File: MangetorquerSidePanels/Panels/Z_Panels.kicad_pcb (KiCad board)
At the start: 6 copper layers, 97 x 97.3 mm, 57 parts, among them J1 SMA Connector Male, J2 Through_Hole_1, Q1 BSS138DWQ-7, Q2 MBT2222ADW1T1, Q3 BSS138DWQ-7, Q4 MBT2222ADW1T1, U1 DRV8830DGQ, U2 BD60GC0WEFJ, U3 HHM1589D1, U4 OPT3001

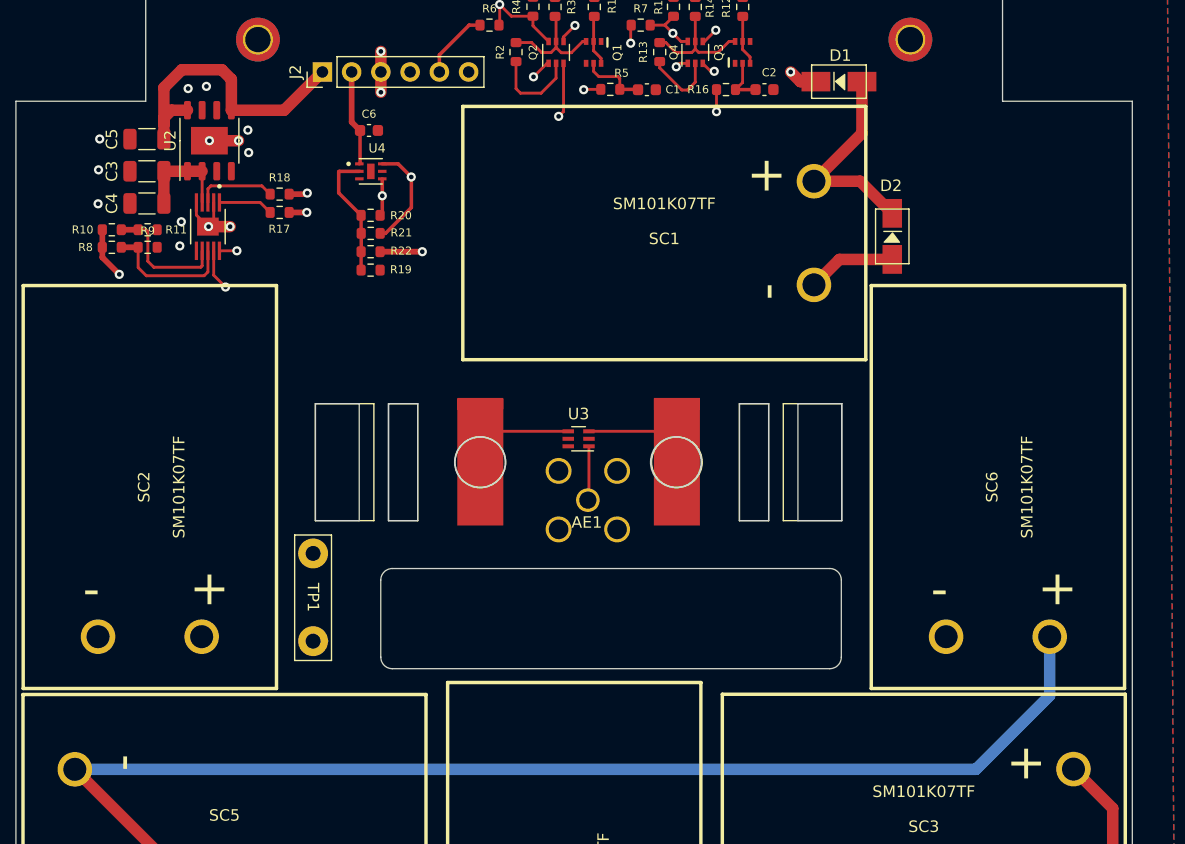
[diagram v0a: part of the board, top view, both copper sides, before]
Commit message: Starting design of magnetorquer side panels
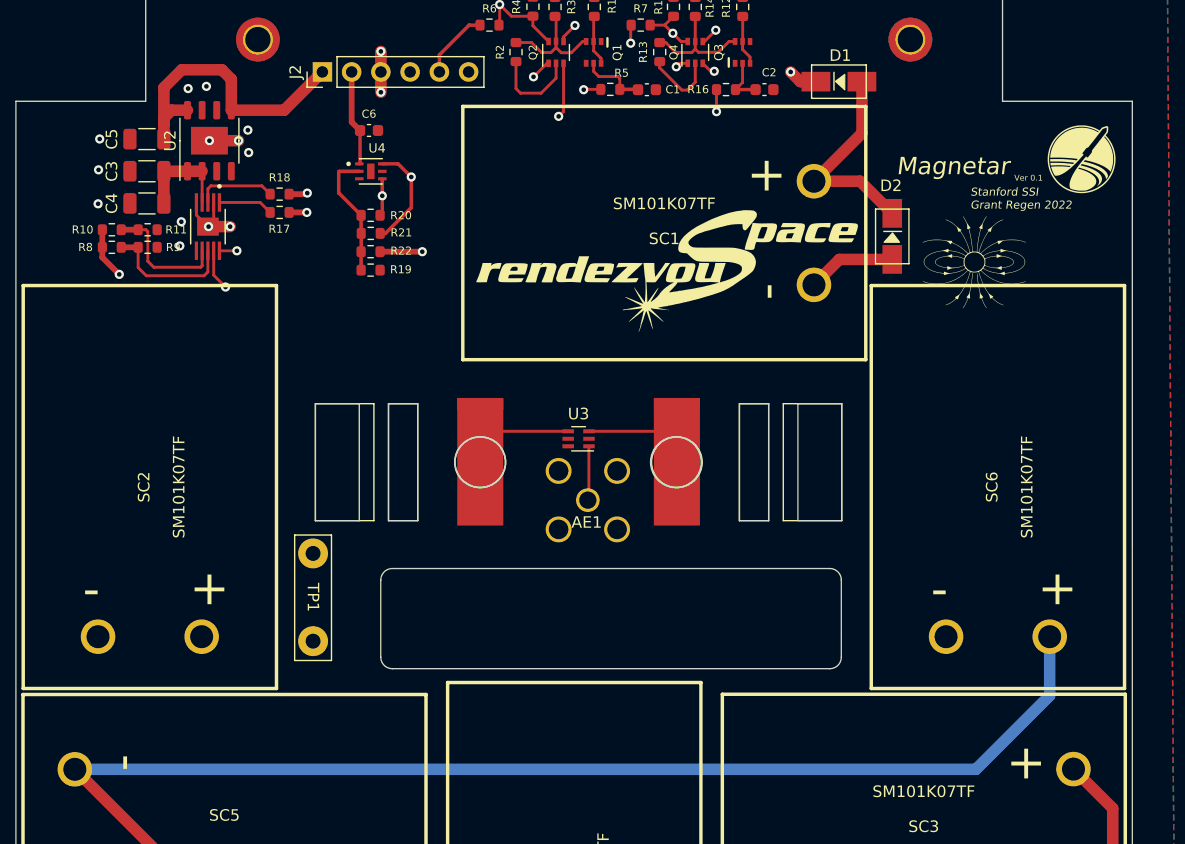
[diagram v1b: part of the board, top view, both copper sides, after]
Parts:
- added REF**: SLAB_logo, panels:SLAB_logo, F.Cu at (190.5, 64.8)
- added REF**: logo_SSI_small, panels:logo_SSI_small, F.Cu at (226.6, 56.6)
- added REF**: logo_magnet_1, panels:logo_magnet_1, F.Cu at (217.4, 65.3)
- added REF**: BAC_logo, panels:BAC_logo, B.Cu at (181.4, 125.5)
- added REF**: logo_SSI, panels:logo_SSI, B.Cu at (182.9, 62.2)
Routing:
- net Coil_OUT: track 46.1 -> 44.9 mm
- net Net-(D6-Pad2): track 123.7 -> 123.1 mm
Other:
- board text added: "Magnetar"
- board text added: "Stanford SSI Grant Regen 2022"
- board text added: "Ver 0.1"

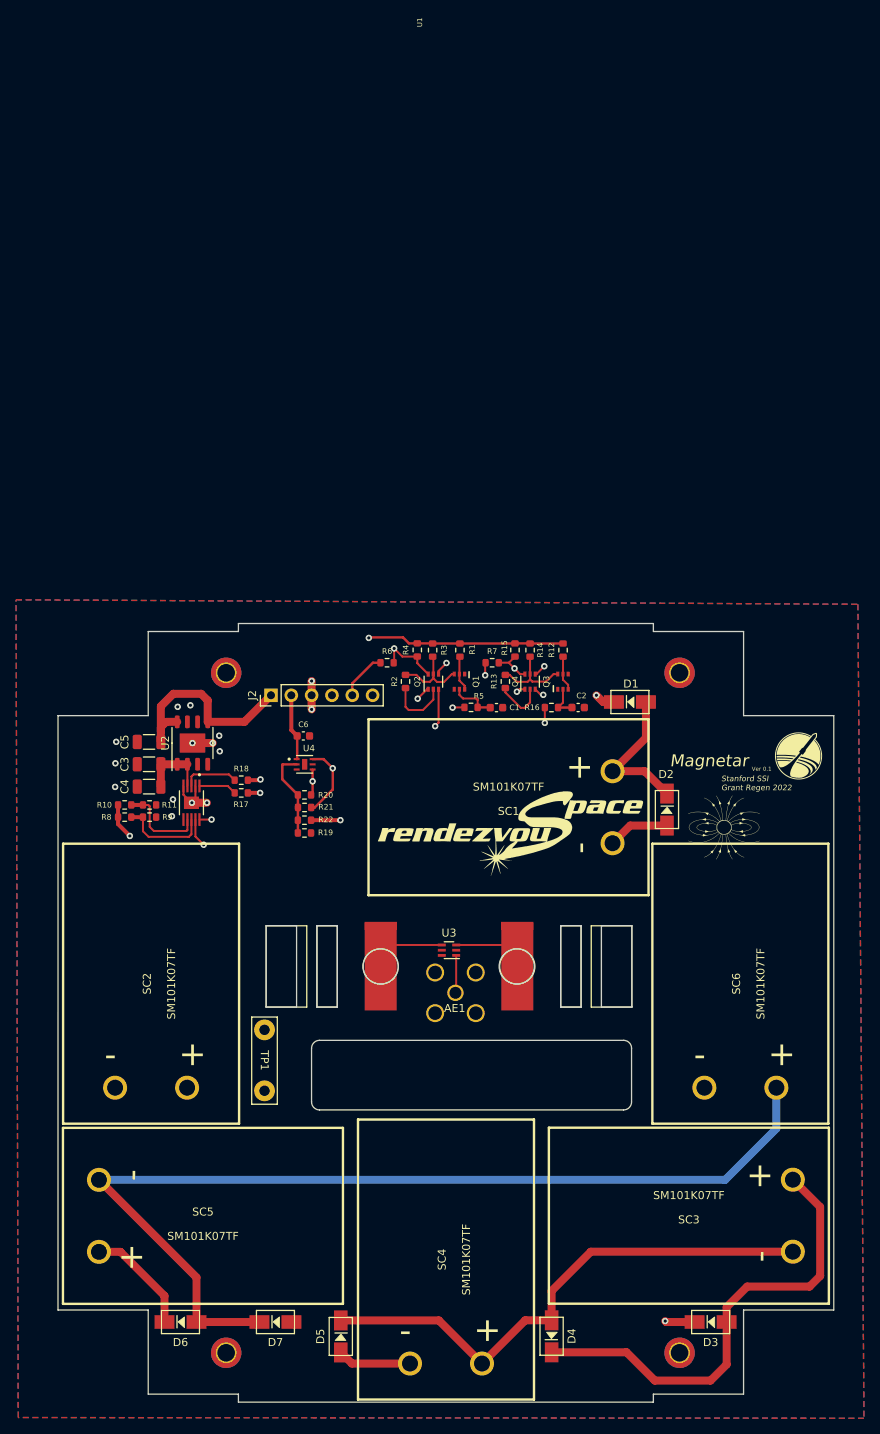
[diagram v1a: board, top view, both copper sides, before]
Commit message: Final flight side panels w/ magnetorquers finished, note final board thickness of 0.031'' and updated copper weight of 0.5oz for internal layers
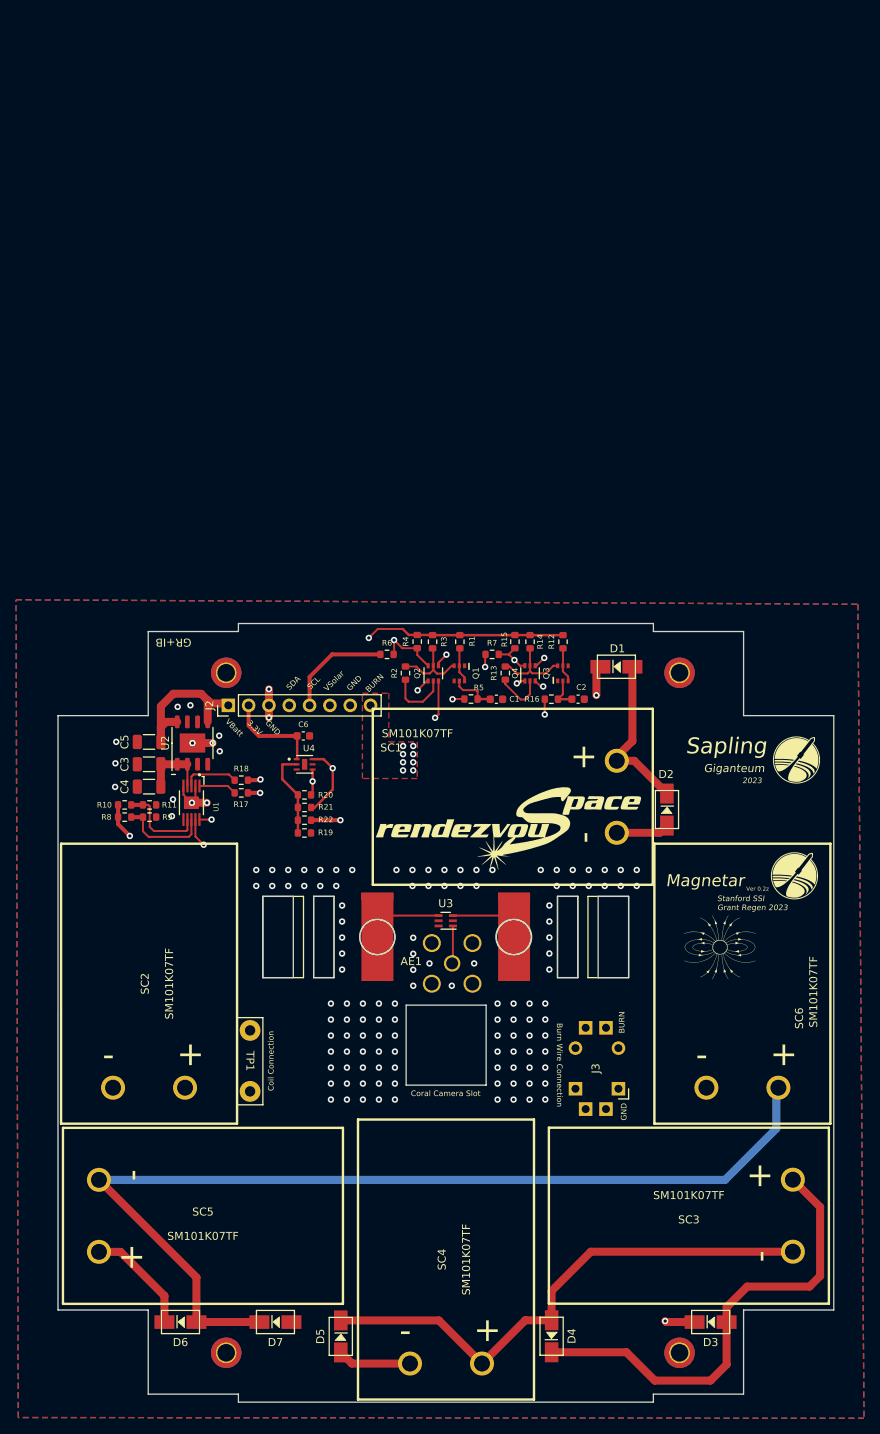
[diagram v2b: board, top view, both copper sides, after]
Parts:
- added J3: Conn_01x02, panels:Burn_Wire_Connection, F.Cu at (206.5, 101.8)
- added REF**: logo_SSI_small, panels:logo_SSI_small, F.Cu at (226.3, 57.1)
- J1: footprint sapling:SMA_Amphenol_901-144_Vertical -> panels:SMA_Amphenol_901-144_Vertical
- J2: value Through_Hole_1 -> Screw_Terminal_01x08; footprint Connector_PinHeader_2.54mm:PinHeader_1x06_P2.54mm_Vertical -> Connector_PinHeader_2.54mm:PinHeader_1x08_P2.54mm_Vertical
- U2: value BD60GC0WEFJ -> BD50GC0WEFJ
- moved REF** 15.0 mm to (226.1, 71.6)
- moved REF** 15.0 mm to (216.9, 80.3)
- moved J2 5.48 mm to (155.4, 50.0)
- moved D1 4.72 mm to (204.0, 45.2)
- moved AE1 3.70 mm to (182.6, 80.3)
- moved J1 3.70 mm to (183.4, 82.3)
- moved U3 3.70 mm to (182.6, 77.0)
- moved TP1 1.81 mm to (157.7, 94.5)
- moved SC1 1.40 mm to (191.0, 61.5)
- moved C2 1.04 mm to (199.2, 49.3)
- moved R1 1.04 mm to (184.4, 42.1)
- moved R12 1.04 mm to (197.3, 42.1)
- moved R14 1.04 mm to (193.2, 42.1)
- moved R16 1.04 mm to (195.8, 49.3)
- moved R3 1.04 mm to (181.0, 42.1)
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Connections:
- R10 pad 1: +3V3 -> VBATT
- R8 pad 1: +3V3 -> VBATT
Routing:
- net +3V3: track 110.3 -> 82.7 mm, vias 3 -> 2
- net VBATT: track 26.2 -> 48.3 mm, vias 0 -> 1
- net BURN: track 0.00 -> 14.0 mm, vias 0 -> 8
- net SCL: track 29.1 -> 41.3 mm
- net SDA: track 33.6 -> 40.8 mm
- net Net-(D1-Pad2): track 18.3 -> 21.3 mm
- net VSOLAR: track 41.0 -> 43.8 mm
- net Coil_IN: track 35.2 -> 32.9 mm
- net SCL_ISO: track 66.6 -> 67.7 mm
- net Coil_OUT: track 44.9 -> 44.2 mm
- net Net-(D2-Pad2): track 154.1 -> 154.6 mm
- net SDA_ISO: track 83.7 -> 84.2 mm
- net GND: vias 15 -> 133
- added copper zone on F.Cu, net BURN
- added copper zone on In3.Cu, net BURN
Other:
- outline, holes or cut-outs redrawn
- board text added: "2023"
- board text added: "3.3V"
- board text added: "BURN"
- board text added: "Burn Wire Connection"
- board text added: "Coil Connection"
- board text added: "Coral Camera Slot"
- board text added: "GND"
- board text added: "Giganteum"
- board text added: "SCL"
- board text added: "SDA"
- board text added: "Sapling"
- board text added: "Stanford SSI Grant Regen 2023"
- board text added: "VBatt"
- board text added: "VSolar"
- board text added: "Ver 0.2z"
- board text removed: "Stanford SSI Grant Regen 2022"
- board text removed: "Ver 0.1"

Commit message: added magnetorquers
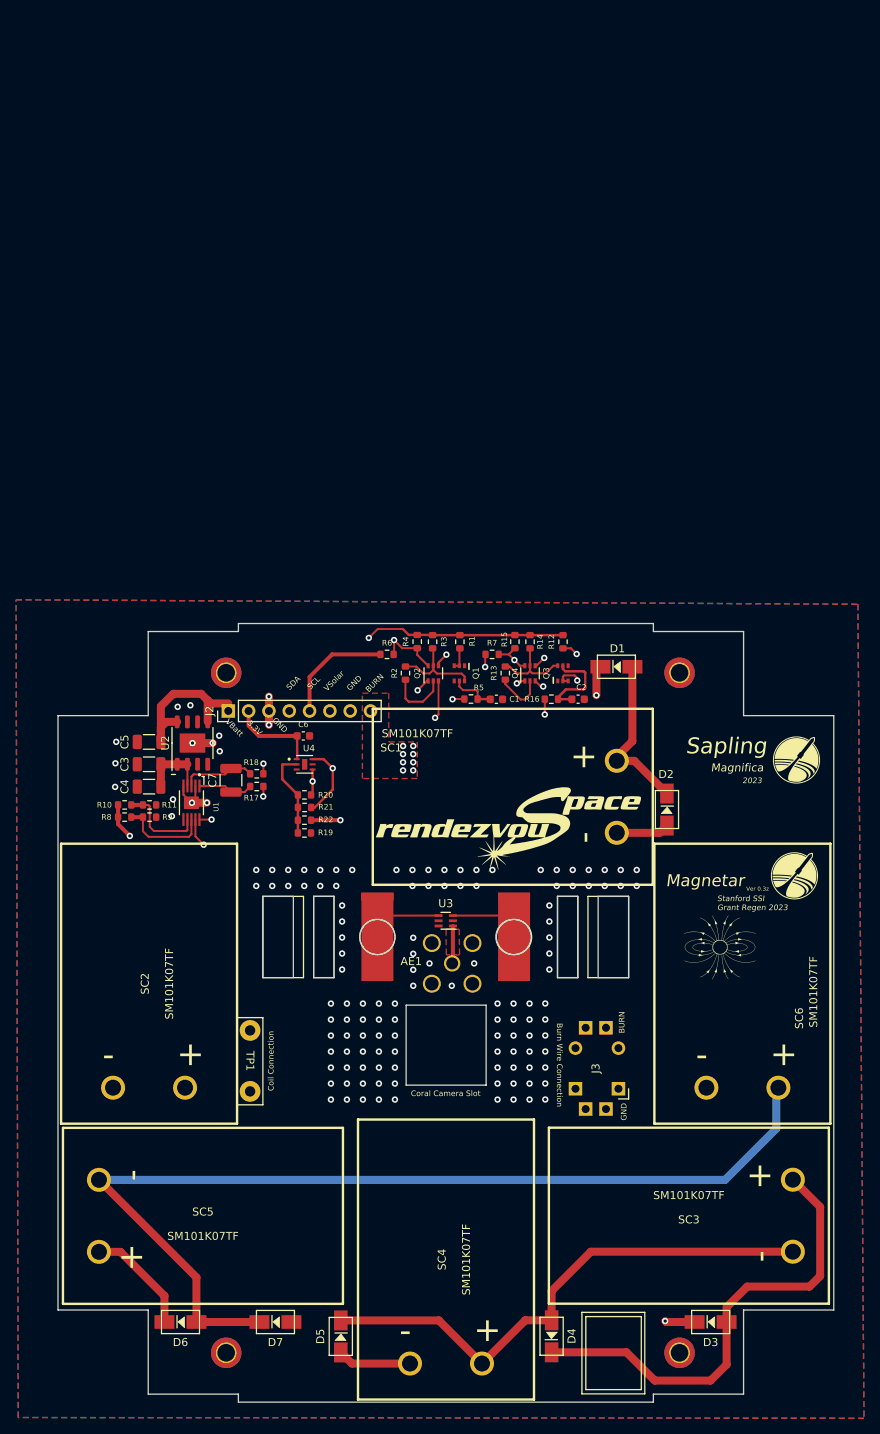
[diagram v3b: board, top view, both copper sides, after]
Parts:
- removed the REF** at (181.4, 125.5)
- added C7: XXuF, Capacitor_SMD:C_1210_3225Metric, F.Cu at (155.8, 59.4)
- moved R17 2.09 mm to (159.0, 60.2)
- moved R18 2.09 mm to (159.0, 58.6)
- moved J2 0.70 mm to (155.4, 50.7)
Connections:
- C2 pad 1: Net-(C2-Pad1) -> Net-(R16-Pad1)
- Q1 pad 2: Net-(Q1-Pad2) -> Net-(R1-Pad1)
- Q1 pad 3: Net-(Q1-Pad3) -> Net-(R1-Pad1)
- Q1 pad 6: Net-(Q1-Pad2) -> Net-(R3-Pad2)
- Q2 pad 5: Net-(Q1-Pad3) -> Net-(R3-Pad2)
- Q3 pad 2: Net-(C2-Pad1) -> Net-(Q3-Pad3)
- Q3 pad 5: Net-(Q3-Pad3) -> Net-(R16-Pad1)
- R1 pad 1: Net-(Q1-Pad2) -> Net-(R1-Pad1)
- R16 pad 1: Net-(C2-Pad1) -> Net-(R16-Pad1)
- R2 pad 1: Net-(Q1-Pad3) -> Net-(R3-Pad2)
- R3 pad 2: Net-(Q1-Pad3) -> Net-(R3-Pad2)
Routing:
- net Net-(R3-Pad2): track 0.00 -> 11.6 mm
- net Net-(R16-Pad1): track 0.00 -> 11.2 mm
- net Net-(Q1-Pad3): track 9.96 -> 0.00 mm
- net Net-(Q3-Pad3): track 4.35 -> 8.94 mm, vias 0 -> 2
- net Net-(Q1-Pad2): track 4.37 -> 0.00 mm
- net Net-(C2-Pad1): track 4.27 -> 0.00 mm
- net Net-(R1-Pad1): track 0.00 -> 2.85 mm
- net +3V3: track 82.7 -> 80.0 mm
- net Net-(R18-Pad1): track 6.99 -> 9.21 mm
- net Net-(R17-Pad1): track 4.76 -> 6.94 mm
- net SCL: track 41.3 -> 43.2 mm
- net SCL_ISO: track 67.7 -> 69.1 mm
- net Coil_OUT: track 44.2 -> 45.3 mm
- net VSOLAR: track 43.8 -> 42.8 mm
- net SDA: track 40.8 -> 41.7 mm
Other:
- board text added: "Magnifica"
- board text added: "Ver 0.3z"
- board text removed: "GR+IB"
- board text removed: "Giganteum"
- board text removed: "Ver 0.2z"
